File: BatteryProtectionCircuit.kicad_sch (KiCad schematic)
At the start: 26 parts, among them J1 Conn_01x07_Pin, Q1 NMOS, U1 LMC555xN, U2 LM358, U3 LM358, U4 LM321

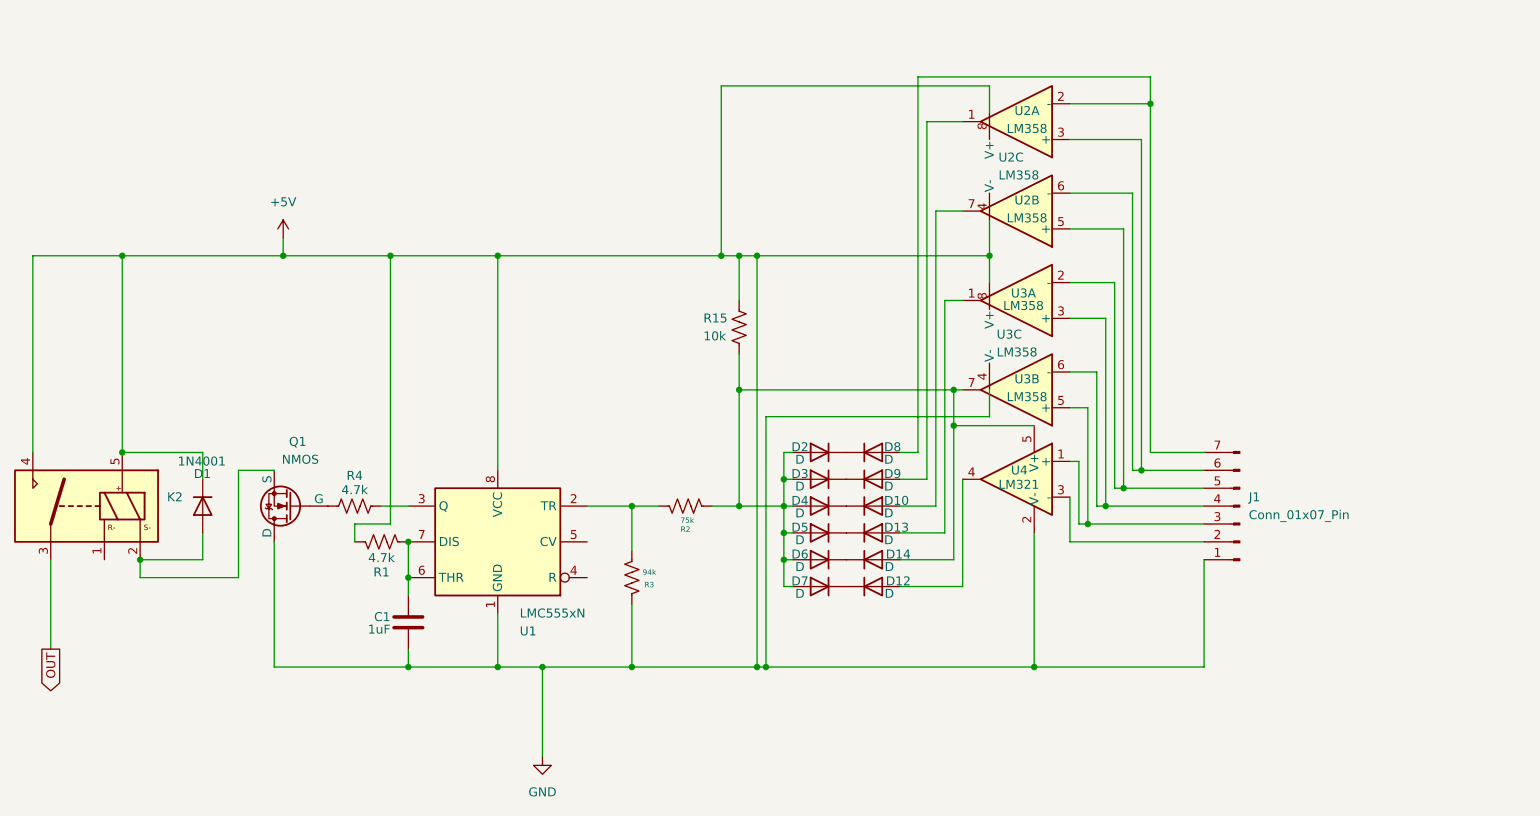
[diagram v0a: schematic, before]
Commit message: Cleaned up circuit so it doesn't explode
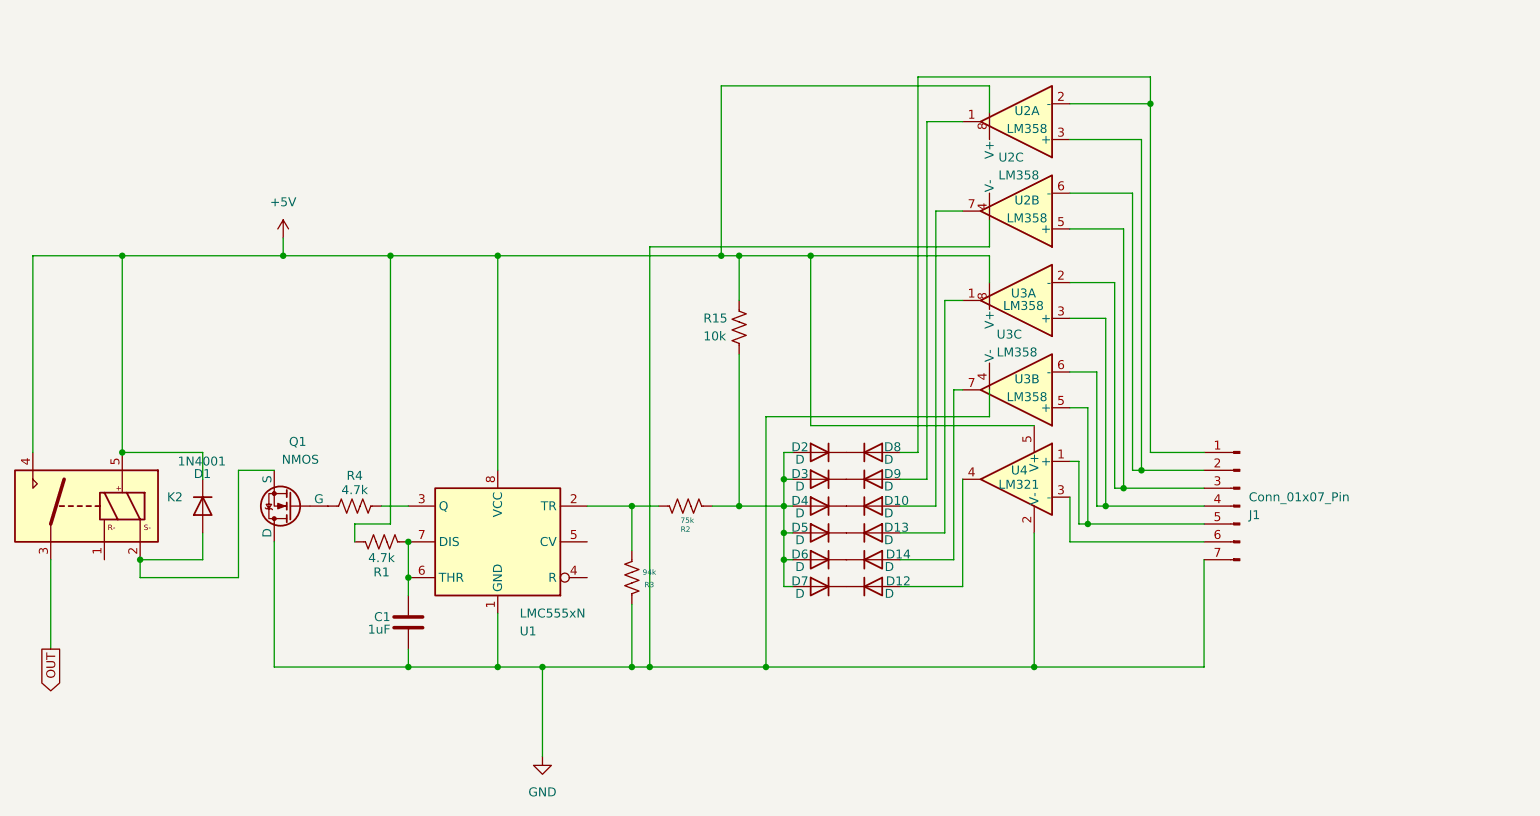
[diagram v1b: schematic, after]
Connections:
- net +5V: now also U4.5 (V+); no longer C1.1, J1.1 (Pin_1), Q1.1 (D), R3.1, U1.1 (GND), U2.4 (V-), U3.4 (V-), U4.2 (V-)
- net at U3.5 (+), U4.1 (+): now also J1.5 (Pin_5); no longer J1.3 (Pin_3)
- net at D2.2 (A), D3.2 (A), D4.2 (A)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: no longer D14.2 (A), U3.7, U4.5 (V+)
- net at U4.3 (-): now also J1.6 (Pin_6); no longer J1.2 (Pin_2)
- net at U2.5 (+), U3.2 (-): now also J1.3 (Pin_3); no longer J1.5 (Pin_5)
- net at U2.3 (+), U2.6 (-): now also J1.2 (Pin_2); no longer J1.6 (Pin_6)
- net at D8.2 (A), U2.2 (-): now also J1.1 (Pin_1); no longer J1.7 (Pin_7)
- new net: D14.2 (A), U3.7
- new net GND: C1.1, J1.7 (Pin_7), Q1.1 (D), R3.1, U1.1 (GND), U2.4 (V-), U3.4 (V-), U4.2 (V-)
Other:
- moved on the sheet: J1
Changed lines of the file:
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@@
-	)
-	(junction
-		(at 151.13 57.15)
-		(diameter 0)
-		(color 0 0 0 0)
 	)
 	(junction
@@
 	)
 	(junction
+		(at 135.89 115.57)
+		(diameter 0)
+		(color 0 0 0 0)
+	)
+	(junction
 		(at 120.65 115.57)
 		(diameter 0)
@@
 	)
 	(junction
-		(at 179.07 76.2)
-		(diameter 0)
-		(color 0 0 0 0)
-	)
-	(junction
-		(at 179.07 81.28)
-		(diameter 0)
-		(color 0 0 0 0)
-	)
-	(junction
-		(at 148.59 76.2)
-		(diameter 0)
-		(color 0 0 0 0)
-	)
-	(junction
 		(at 152.4 115.57)
 		(diameter 0)
@@
 	)
 	(junction
-		(at 151.13 115.57)
-		(diameter 0)
-		(color 0 0 0 0)
-	)
-	(junction
 		(at 133.35 92.71)
 		(diameter 0)
@@
 	)
 	(junction
-		(at 184.15 57.15)
-		(diameter 0)
-		(color 0 0 0 0)
-	)
-	(junction
 		(at 190.5 115.57)
 		(diameter 0)
@@
 	)
 	(junction
+		(at 158.75 57.15)
+		(diameter 0)
+		(color 0 0 0 0)
+	)
+	(junction
 		(at 154.94 100.33)
 		(diameter 0)
@@
 	(wire
 		(pts
-			(xy 179.07 81.28) (xy 179.07 100.33)
+			(xy 179.07 76.2) (xy 179.07 100.33)
 		)
 		(stroke
@@
 	(wire
 		(pts
-			(xy 148.59 76.2) (xy 179.07 76.2)
-		)
-		(stroke
-			(width 0)
-			(type default)
-		)
-	)
-	(wire
-		(pts
 			(xy 93.98 97.79) (xy 93.98 95.25)
 		)
@@
 	(wire
 		(pts
-			(xy 151.13 57.15) (xy 184.15 57.15)
-		)
-		(stroke
-			(width 0)
-			(type default)
-		)
-	)
-	(wire
-		(pts
 			(xy 195.58 35.56) (xy 207.01 35.56)
 		)
@@
 	(wire
 		(pts
-			(xy 148.59 76.2) (xy 148.59 92.71)
-		)
-		(stroke
-			(width 0)
-			(type default)
-		)
-	)
-	(wire
-		(pts
 			(xy 173.99 85.09) (xy 171.45 85.09)
 		)
@@
 	(wire
 		(pts
-			(xy 184.15 57.15) (xy 184.15 60.96)
-		)
-		(stroke
-			(width 0)
-			(type default)
-		)
-	)
-	(wire
-		(pts
 			(xy 177.8 63.5) (xy 177.8 96.52)
 		)
@@
 	(wire
 		(pts
+			(xy 184.15 57.15) (xy 158.75 57.15)
+		)
+		(stroke
+			(width 0)
+			(type default)
+		)
+	)
+	(wire
+		(pts
 			(xy 154.94 96.52) (xy 156.21 96.52)
 		)
@@
 	(wire
 		(pts
-			(xy 133.35 115.57) (xy 151.13 115.57)
+			(xy 133.35 115.57) (xy 135.89 115.57)
 		)
 		(stroke
@@
 	(wire
 		(pts
+			(xy 158.75 81.28) (xy 158.75 57.15)
+		)
+		(stroke
+			(width 0)
+			(type default)
+		)
+	)
+	(wire
+		(pts
 			(xy 180.34 76.2) (xy 179.07 76.2)
 		)
@@
 	(wire
 		(pts
-			(xy 184.15 52.07) (xy 184.15 57.15)
-		)
-		(stroke
-			(width 0)
-			(type default)
-		)
-	)
-	(wire
-		(pts
 			(xy 200.66 66.04) (xy 195.58 66.04)
 		)
@@
 	(wire
 		(pts
+			(xy 184.15 55.88) (xy 135.89 55.88)
+		)
+		(stroke
+			(width 0)
+			(type default)
+		)
+	)
+	(wire
+		(pts
 			(xy 180.34 63.5) (xy 177.8 63.5)
 		)
@@
 	(wire
 		(pts
+			(xy 135.89 55.88) (xy 135.89 115.57)
+		)
+		(stroke
+			(width 0)
+			(type default)
+		)
+	)
+	(wire
+		(pts
 			(xy 184.15 80.01) (xy 152.4 80.01)
 		)
@@
 	(wire
 		(pts
-			(xy 190.5 81.28) (xy 179.07 81.28)
-		)
-		(stroke
-			(width 0)
-			(type default)
-		)
-	)
-	(wire
-		(pts
 			(xy 176.53 50.8) (xy 176.53 92.71)
 		)
@@
 	(wire
 		(pts
-			(xy 179.07 81.28) (xy 179.07 76.2)
-		)
-		(stroke
-			(width 0)
-			(type default)
-		)
-	)
-	(wire
-		(pts
 			(xy 214.63 100.33) (xy 214.63 115.57)
 		)
@@
 	(wire
 		(pts
-			(xy 148.59 57.15) (xy 151.13 57.15)
+			(xy 148.59 57.15) (xy 158.75 57.15)
 		)
 		(stroke
@@
 	(wire
 		(pts
-			(xy 148.59 76.2) (xy 148.59 71.12)
+			(xy 148.59 71.12) (xy 148.59 92.71)
 		)
 		(stroke
@@
 	(wire
 		(pts
-			(xy 151.13 115.57) (xy 152.4 115.57)
+			(xy 135.89 115.57) (xy 152.4 115.57)
 		)
 		(stroke
@@
 	(wire
 		(pts
+			(xy 184.15 60.96) (xy 184.15 57.15)
+		)
+		(stroke
+			(width 0)
+			(type default)
+		)
+	)
+	(wire
+		(pts
 			(xy 154.94 85.09) (xy 154.94 88.9)
 		)
@@
 	(wire
 		(pts
+			(xy 190.5 81.28) (xy 158.75 81.28)
+		)
+		(stroke
+			(width 0)
+			(type default)
+		)
+	)
+	(wire
+		(pts
 			(xy 205.74 87.63) (xy 214.63 87.63)
 		)
@@
 	(wire
 		(pts
-			(xy 151.13 57.15) (xy 151.13 115.57)
+			(xy 184.15 52.07) (xy 184.15 55.88)
 		)
 		(stroke
@@
 	(symbol
 		(lib_id "Connector:Conn_01x07_Pin")
-		(at 219.71 92.71 180)
+		(at 219.71 92.71 0)
+		(mirror y)
 		(unit 1)
 		(exclude_from_sim no)
@@
 		(on_board yes)
 		(dnp no)
-		(fields_autoplaced yes)
 		(property "Reference" "J1"
-			(at 220.98 91.4399 0)
+			(at 220.98 93.9801 0)
 			(effects
 				(font
@@
 		)
 		(property "Value" "Conn_01x07_Pin"
-			(at 220.98 93.9799 0)
-			(effects
-				(font
+			(at 220.98 91.4401 0)
+			(effects
+				(font

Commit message: Update BatteryProtectionCircuit.kicad_sch
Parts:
- removed D10, D12, D13, D2, D3, D4, D5, D6, D7, D8, D9: D, Diode_SMD:D_0805_2012Metric, symbol Device:D
- removed D14: D, Connector_PinHeader_1.00mm:PinHeader_1x02_P1.00mm_Vertical_SMD_Pin1Left, symbol Device:D
- removed J1: Conn_01x07_Pin, Connector_JST:JST_XH_B7B-XH-AM_1x07_P2.50mm_Vertical, symbol Connector:Conn_01x07_Pin
- removed R15: 10k, Resistor_SMD:R_0805_2012Metric, symbol Device:R_US
- removed R2: 75k, Resistor_SMD:R_0805_2012Metric, symbol Device:R_US
- removed R3: 94k, Resistor_SMD:R_0805_2012Metric, symbol Device:R_US
- removed U1: LMC555xN, Package_DIP:DIP-8_W7.62mm, symbol Timer:LMC555xN
- added C2: 1uF, Capacitor_SMD:C_0805_2012Metric, symbol Device:C
- added D2, D3, D4, D5, D6, D7: SS14, Diode_SMD:D_SMA, symbol Diode:SS14
- added J2: Conn_01x07_Pin, Connector_JST:JST_XH_B7B-XH-AM_1x07_P2.50mm_Vertical, symbol Connector:Conn_01x07_Pin
- added R10, R11, R12, R13, R14, R16, R17, R18, R19, R20, R21, R22, R23, R24, R25, R5, R6, R7, R8, R9: 10K, Resistor_SMD:R_0805_2012Metric, symbol Device:R_US
- added R26: 4.7k, Resistor_SMD:R_0805_2012Metric, symbol Device:R_US
- added R27: 200k, Resistor_SMD:R_0805_2012Metric, symbol Device:R_US
- added R28: 75k, Resistor_SMD:R_0805_2012Metric, symbol Device:R_US
- added U6: LMC555xN, Package_DIP:DIP-8_W7.62mm, symbol Timer:LMC555xN
- K2: footprint (none) -> Relay_THT:Relay_SPDT_Panasonic_DR-L
- R1: value 4.7k -> 10k
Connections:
- net GND: now also C1.2, C2.1, J2.7 (Pin_7), R12.2, R16.2, R19.2, R22.2, R27.1, R8.2, U6.1 (GND); no longer C1.1
- net OUT: now also R4.1, U6.3 (Q)
- net REL: now reaches D1.2 (A), Q1.3 (S)
- net REL: now also K2.1; no longer K2.2
- net at U3.5 (+): now also R18.1, R19.1; no longer U4.1 (+)
- net at U3.3 (+): now also R14.1, R16.1; no longer U3.6 (-)
- net D50: now reaches U3.7
- net D50: now also D6.1 (K), R24.1
- net at U4.3 (-): now also R20.1, R25.2
- net D60: now reaches U4.4
- net D60: now also D7.1 (K), R25.1
- net at U2.5 (+): now also R11.1, R12.1; no longer U3.2 (-)
- net at U2.3 (+): now also R7.1, R8.1; no longer U2.6 (-)
- net D30: now reaches U2.7
- net D30: now also D4.1 (K), R10.1
- net at U2.2 (-): now also R5.1, R6.2
- net VD: now reaches R1.2
- net VD: now also D2.2 (A), D3.2 (A), D4.2 (A), D5.2 (A), D6.2 (A), D7.2 (A), R28.2; no longer C1.2
- net D40: now reaches U3.1
- net D40: now also D5.1 (K), R23.1
- net D20: now reaches U2.1
- net D20: now also D3.1 (K), R6.1
- net +5V renamed VIN
- net VIN: now also R26.1, U6.4 (R), U6.8 (VCC)
- new net: R17.1, R24.2, U3.6 (-)
- new net: C1.1, U6.5 (CV)
- new net: R21.1, R22.1, U4.1 (+)
- new net: R10.2, R9.1, U2.6 (-)
- new net: R13.1, R23.2, U3.2 (-)
- new net: C2.2, R26.2, U6.6 (THR), U6.7 (DIS)
- new net D10: D2.1 (K), J2.1 (Pin_1), R5.2
- new net D12: J2.2 (Pin_2), R7.2, R9.2
- new net D22: J2.3 (Pin_3), R11.2, R13.2
- new net D32: J2.4 (Pin_4), R14.2, R17.2
- new net D42: J2.5 (Pin_5), R18.2, R20.2
- new net D52: J2.6 (Pin_6), R21.2
- new net TR: R27.2, R28.1, U6.2 (TR)
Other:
- note added: "7 Pin Power Connection"
- note added: "Analog Diode OR Network"
- note added: "Circuit Breaking Latching Relay"
- note added: "Differential Op-Amp Array"
- note added: "Monotable 555 Timer"
- note added: "Mosfet Driver (for relay)"
- note added: "Voltage Divider"
- moved on the sheet: D1, K2, Q1, R4, U2A, U2B, U2C, U3A, U3B, U3C, U4

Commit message: Footprints + PCB
Added footprints to schematic and started with preliminary PCB layout and routing, likely to change.
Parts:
- K2: footprint Relay_THT:Relay_SPDT_Panasonic_DR-L -> Relay_THT:Relay_SPDT_Panasonic_JW1_FormC
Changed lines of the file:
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@@
 			)
 		)
-		(property "Footprint" "Relay_THT:Relay_SPDT_Panasonic_DR-L"
+		(property "Footprint" "Relay_THT:Relay_SPDT_Panasonic_JW1_FormC"
 			(at 146.05 41.91 0)
 			(effects

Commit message: Switched Relay
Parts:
- K2: footprint Relay_THT:Relay_SPDT_Panasonic_JW1_FormC -> New Relay:CONN5_21105_PAN
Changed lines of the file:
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@@
 			)
 		)
-		(property "Footprint" "Relay_THT:Relay_SPDT_Panasonic_JW1_FormC"
+		(property "Footprint" "New Relay:CONN5_21105_PAN"
 			(at 146.05 41.91 0)
 			(effects

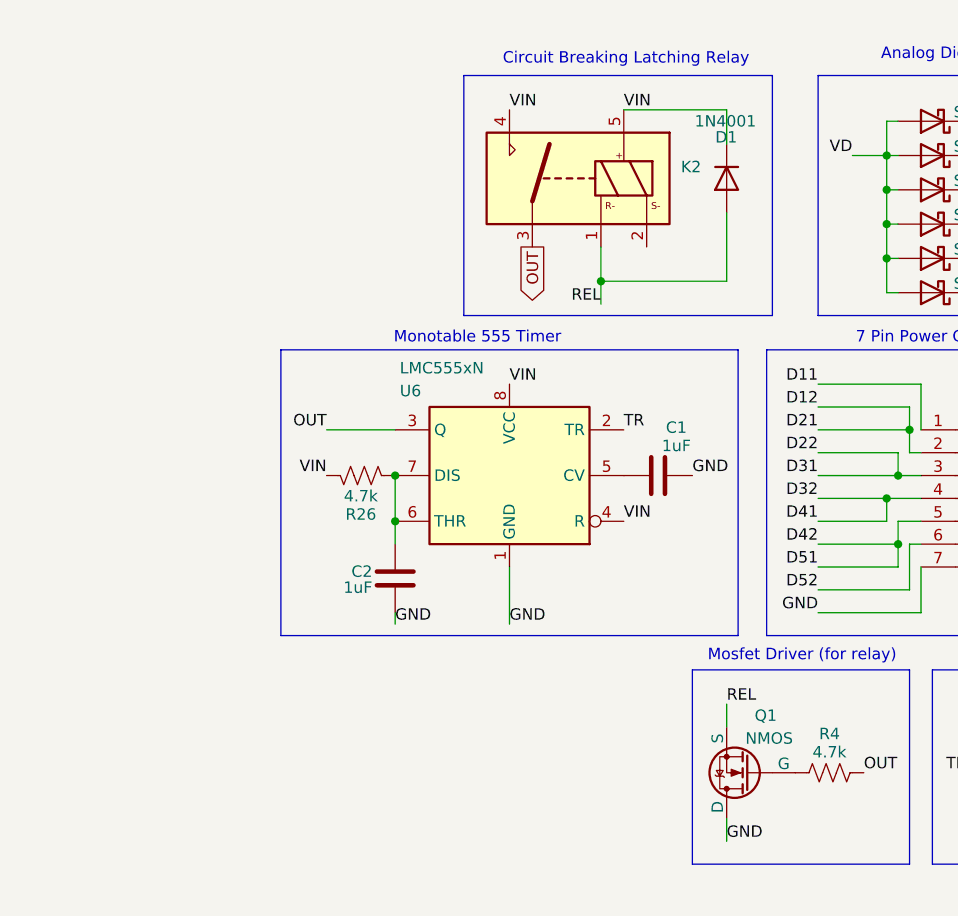
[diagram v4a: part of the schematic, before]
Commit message: Added Connectors for power rail and robot input
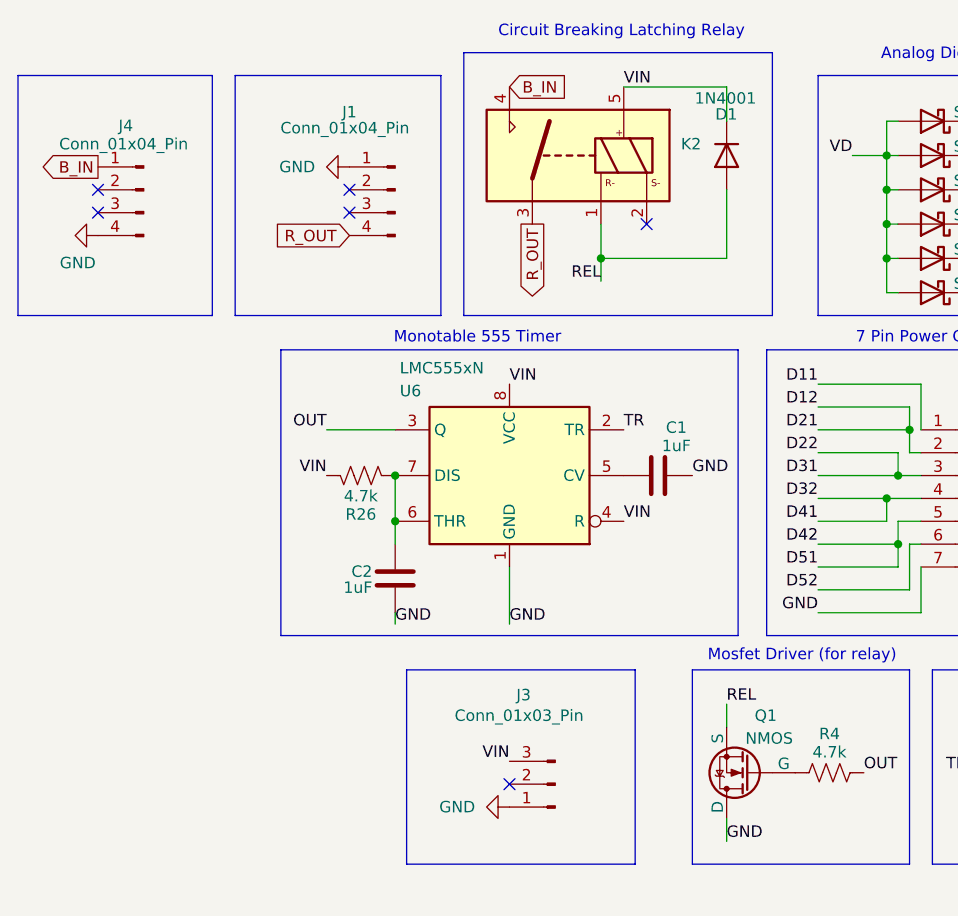
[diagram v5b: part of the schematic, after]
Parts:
- added J1, J4: Conn_01x04_Pin, footprints:CONN2_2606-1102_WAG, symbol Connector:Conn_01x04_Pin
- added J3: Conn_01x03_Pin, Connector_JST:JST_XH_B3B-XH-AM_1x03_P2.50mm_Vertical, symbol Connector:Conn_01x03_Pin
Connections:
- net GND: now also J1.1 (Pin_1), J3.1 (Pin_1), J4.4 (Pin_4)
- net OUT: no longer K2.3
- net VIN: now also J3.3 (Pin_3); no longer K2.4
- new net B_IN: J4.1 (Pin_1), K2.4
- new net R_OUT: J1.4 (Pin_4), K2.3
- no-connect marks 0 -> 6
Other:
- moved on the sheet: D1, K2
